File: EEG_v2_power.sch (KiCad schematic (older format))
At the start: 17 parts, among them U2 TLV70033, U3 LM2664, U4 TLV70025, U5 TPS72325

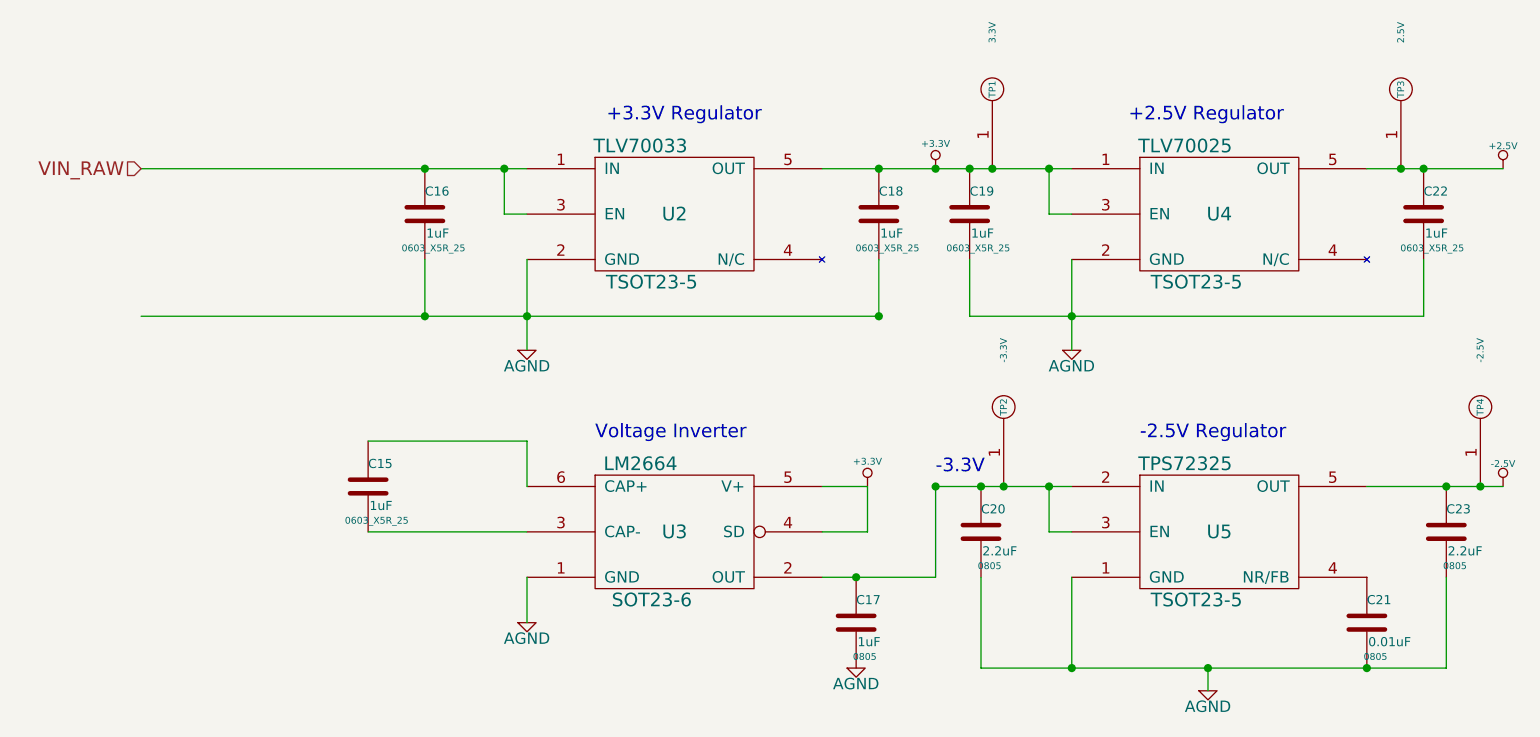
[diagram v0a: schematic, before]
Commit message: Added footprints to connectors. Changed usb A to usb micro B
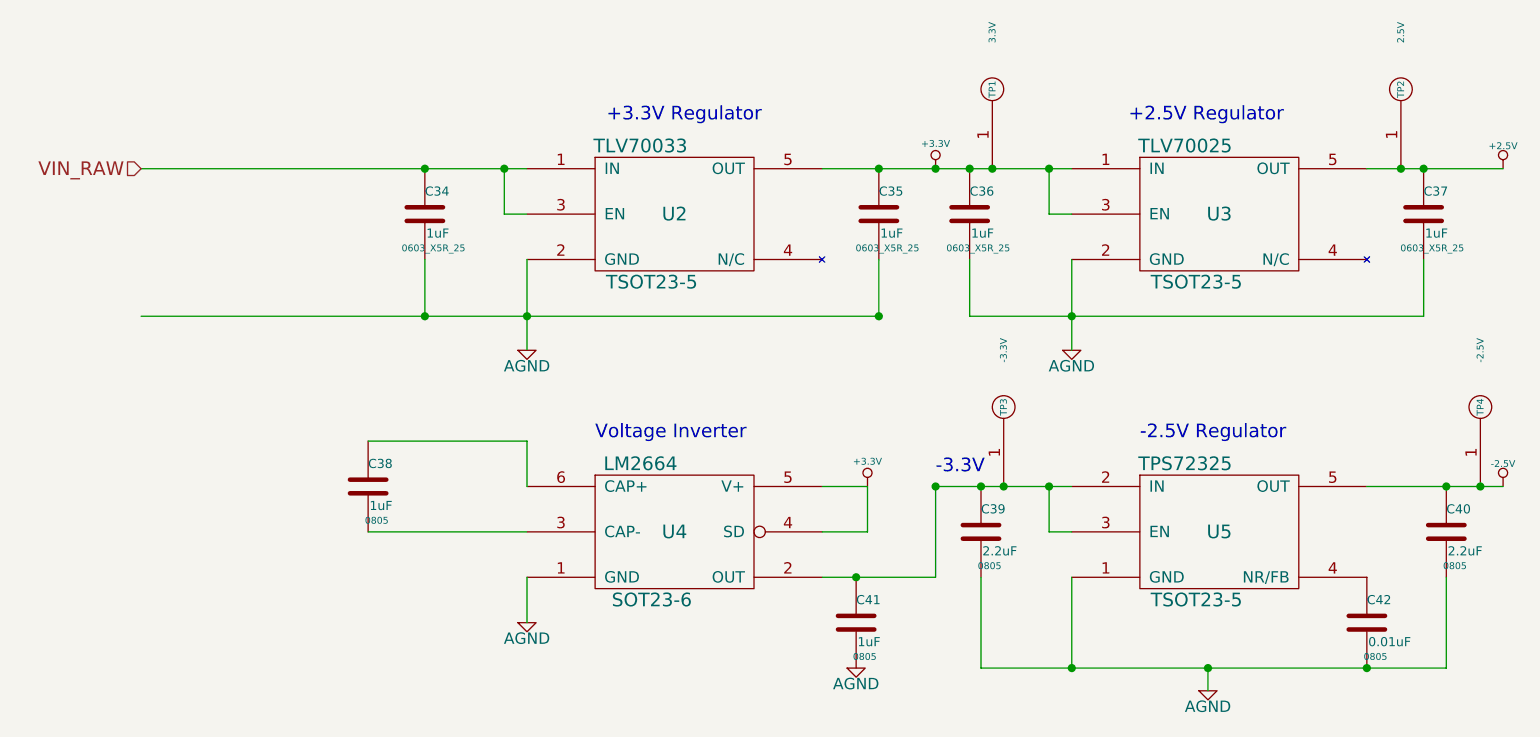
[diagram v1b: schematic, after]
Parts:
- C38: renamed from C15; footprint 0603_X5R_25 -> 0805
- renumbered C16 to C34, C18 to C35, C19 to C36, C22 to C37, C20 to C39, C23 to C40, C17 to C41, C21 to C42, TP3 to TP2, TP2 to TP3, U4 to U3, U3 to U4
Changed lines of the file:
@@
 $EndDescr
 $Comp
-L LM2664 U3
+L LM2664 U4
 U 1 1 54B47F36
 P 5300 4650
-F 0 "U3" H 5300 4650 60  0000 C CNN
+F 0 "U4" H 5300 4650 60  0000 C CNN
 F 1 "LM2664" H 5150 4950 60  0000 C CNN
 F 2 "SOT23-6" H 5200 4350 60  0000 C CNN
@@
 $EndComp
 $Comp
-L TLV70025 U4
+L TLV70025 U3
 U 1 1 54B47F3C
 P 7700 3250
-F 0 "U4" H 7700 3250 60  0000 C CNN
+F 0 "U3" H 7700 3250 60  0000 C CNN
 F 1 "TLV70025" H 7550 3550 60  0000 C CNN
 F 2 "TSOT23-5" H 7600 2950 60  0000 C CNN
@@
 $EndComp
 $Comp
-L C C16
+L C C34
 U 1 1 54B47F5B
 P 4200 3250
-F 0 "C16" H 4200 3350 40  0000 L CNN
+F 0 "C34" H 4200 3350 40  0000 L CNN
 F 1 "1uF" H 4206 3165 40  0000 L CNN
 F 2 "0603_X5R_25" H 4238 3100 30  0000 C CNN
@@
 $EndComp
 $Comp
-L C C18
+L C C35
 U 1 1 54B47F61
 P 6200 3250
-F 0 "C18" H 6200 3350 40  0000 L CNN
+F 0 "C35" H 6200 3350 40  0000 L CNN
 F 1 "1uF" H 6206 3165 40  0000 L CNN
 F 2 "0603_X5R_25" H 6238 3100 30  0000 C CNN
@@
 $EndComp
 $Comp
-L C C19
+L C C36
 U 1 1 54B47F67
 P 6600 3250
-F 0 "C19" H 6600 3350 40  0000 L CNN
+F 0 "C36" H 6600 3350 40  0000 L CNN
 F 1 "1uF" H 6606 3165 40  0000 L CNN
 F 2 "0603_X5R_25" H 6638 3100 30  0000 C CNN
@@
 $EndComp
 $Comp
-L C C22
+L C C37
 U 1 1 54B47F73
 P 8600 3250
-F 0 "C22" H 8600 3350 40  0000 L CNN
+F 0 "C37" H 8600 3350 40  0000 L CNN
 F 1 "1uF" H 8606 3165 40  0000 L CNN
 F 2 "0603_X5R_25" H 8638 3100 30  0000 C CNN
@@
 +2.5V Regulator
 $Comp
-L C C15
+L C C38
 U 1 1 54B47F80
 P 3950 4450
-F 0 "C15" H 3950 4550 40  0000 L CNN
+F 0 "C38" H 3950 4550 40  0000 L CNN
 F 1 "1uF" H 3956 4365 40  0000 L CNN
-F 2 "0603_X5R_25" H 3988 4300 30  0000 C CNN
+F 2 "0805" H 3988 4300 30  0000 C CNN
 F 3 "~" H 3950 4450 60  0000 C CNN
 	1    3950 4450
@@
 $EndComp
 $Comp
-L C C17
+L C C41
 U 1 1 54B47F8C
 P 6100 5050
-F 0 "C17" H 6100 5150 40  0000 L CNN
+F 0 "C41" H 6100 5150 40  0000 L CNN
 F 1 "1uF" H 6106 4965 40  0000 L CNN
 F 2 "0805" H 6138 4900 30  0000 C CNN
@@
 -3.3V
 $Comp
-L C C20
+L C C39
 U 1 1 54B47FA0
 P 6650 4650
-F 0 "C20" H 6650 4750 40  0000 L CNN
+F 0 "C39" H 6650 4750 40  0000 L CNN
 F 1 "2.2uF" H 6656 4565 40  0000 L CNN
 F 2 "0805" H 6688 4500 30  0000 C CNN
@@
 $EndComp
 $Comp
-L C C23
+L C C40
 U 1 1 54B47FA6
 P 8700 4650
-F 0 "C23" H 8700 4750 40  0000 L CNN
+F 0 "C40" H 8700 4750 40  0000 L CNN
 F 1 "2.2uF" H 8706 4565 40  0000 L CNN
 F 2 "0805" H 8738 4500 30  0000 C CNN
@@
 $EndComp
 $Comp
-L C C21
+L C C42
 U 1 1 54B47FAC
 P 8350 5050
-F 0 "C21" H 8350 5150 40  0000 L CNN
+F 0 "C42" H 8350 5150 40  0000 L CNN
 F 1 "0.01uF" H 8356 4965 40  0000 L CNN
 F 2 "0805" H 8388 4900 30  0000 C CNN
@@
 $EndComp
 $Comp
-L SMD_1PIN_PAD TP3
+L SMD_1PIN_PAD TP2
 U 1 1 54C4B7DE
 P 8500 2700
-F 0 "TP3" H 8500 2700 30  0000 C CNN
+F 0 "TP2" H 8500 2700 30  0000 C CNN
 F 1 "2.5V" H 8750 2700 30  0000 C CNN
 F 2 "~" H 8500 2700 60  0000 C CNN
@@
 $EndComp
 $Comp
-L SMD_1PIN_PAD TP2
+L SMD_1PIN_PAD TP3
 U 1 1 54C4B7E9
 P 6750 4100
-F 0 "TP2" H 6750 4100 30  0000 C CNN
+F 0 "TP3" H 6750 4100 30  0000 C CNN
 F 1 "-3.3V" H 7000 4100 30  0000 C CNN
 F 2 "~" H 6750 4100 60  0000 C CNN

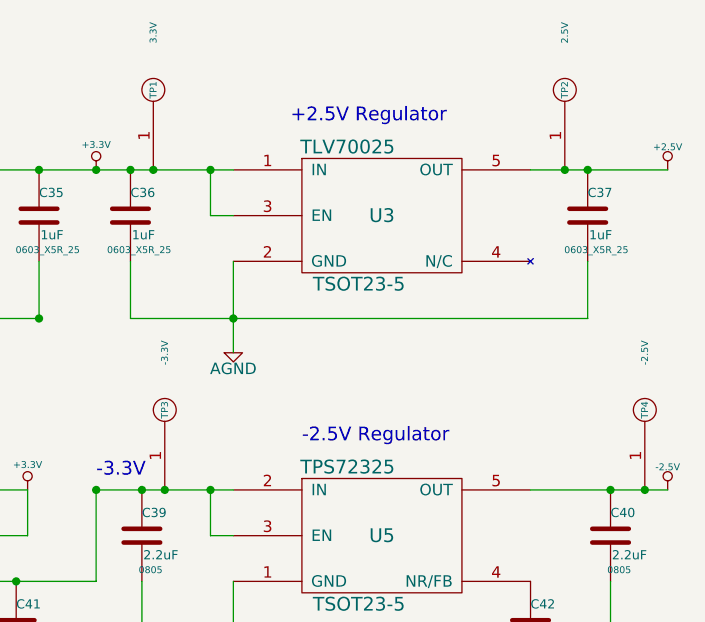
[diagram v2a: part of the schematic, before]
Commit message: Add datasheet for power switch, footprints for test points
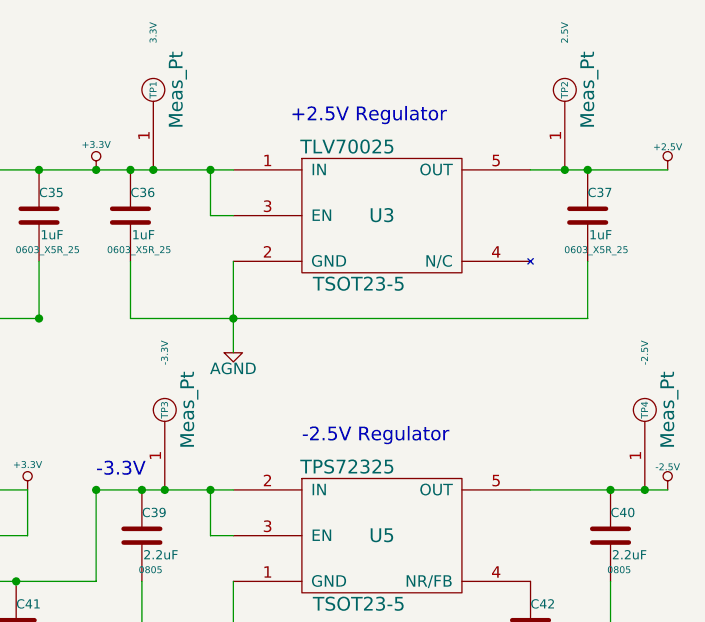
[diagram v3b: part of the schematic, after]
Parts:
- TP1, TP2, TP3, TP4: footprint ~ -> Meas_Pt
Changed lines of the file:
@@
 F 0 "TP1" H 6700 2700 30  0000 C CNN
 F 1 "3.3V" H 6950 2700 30  0000 C CNN
-F 2 "~" H 6700 2700 60  0000 C CNN
+F 2 "Meas_Pt" H 6700 2600 60  0000 C CNN
 F 3 "~" H 6700 2700 60  0000 C CNN
 	1    6700 2700
@@
 F 0 "TP2" H 8500 2700 30  0000 C CNN
 F 1 "2.5V" H 8750 2700 30  0000 C CNN
-F 2 "~" H 8500 2700 60  0000 C CNN
+F 2 "Meas_Pt" H 8500 2600 60  0000 C CNN
 F 3 "~" H 8500 2700 60  0000 C CNN
 	1    8500 2700
@@
 F 0 "TP3" H 6750 4100 30  0000 C CNN
 F 1 "-3.3V" H 7000 4100 30  0000 C CNN
-F 2 "~" H 6750 4100 60  0000 C CNN
+F 2 "Meas_Pt" H 6750 4000 60  0000 C CNN
 F 3 "~" H 6750 4100 60  0000 C CNN
 	1    6750 4100
@@
 F 0 "TP4" H 8850 4100 30  0000 C CNN
 F 1 "-2.5V" H 9100 4100 30  0000 C CNN
-F 2 "~" H 8850 4100 60  0000 C CNN
+F 2 "Meas_Pt" H 8850 4000 60  0000 C CNN
 F 3 "~" H 8850 4100 60  0000 C CNN
 	1    8850 4100

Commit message: Continued layout work.
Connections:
- net N3.3V: now reaches C39.1, C41.1, TP3.1, U4.2 (OUT), U5.2 (IN), U5.3 (EN)
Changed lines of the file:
@@
 	4550 3250 4550 3050
 Connection ~ 4550 3050
+Text Label 6850 4450 0    60   ~ 0
+N3.3V
 $EndSCHEMATC
